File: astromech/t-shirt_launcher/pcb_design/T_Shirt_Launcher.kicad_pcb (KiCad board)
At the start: 2 copper layers, 15 parts, among them J1 Conn_01x02_Socket, J2 Conn_01x02_Socket, U1 ESP32-C6-DEVKITC-1-N8, U2 D36V50F5_Pololu, U3 ADA4510-2ARZ, U4 ADA4510-2ARZ, U5 MAX22203AUU+, U6 ADP3634ARDZ, U7 SN74LVC1G19DBVR, U8 SN74LVC1G19DBVR

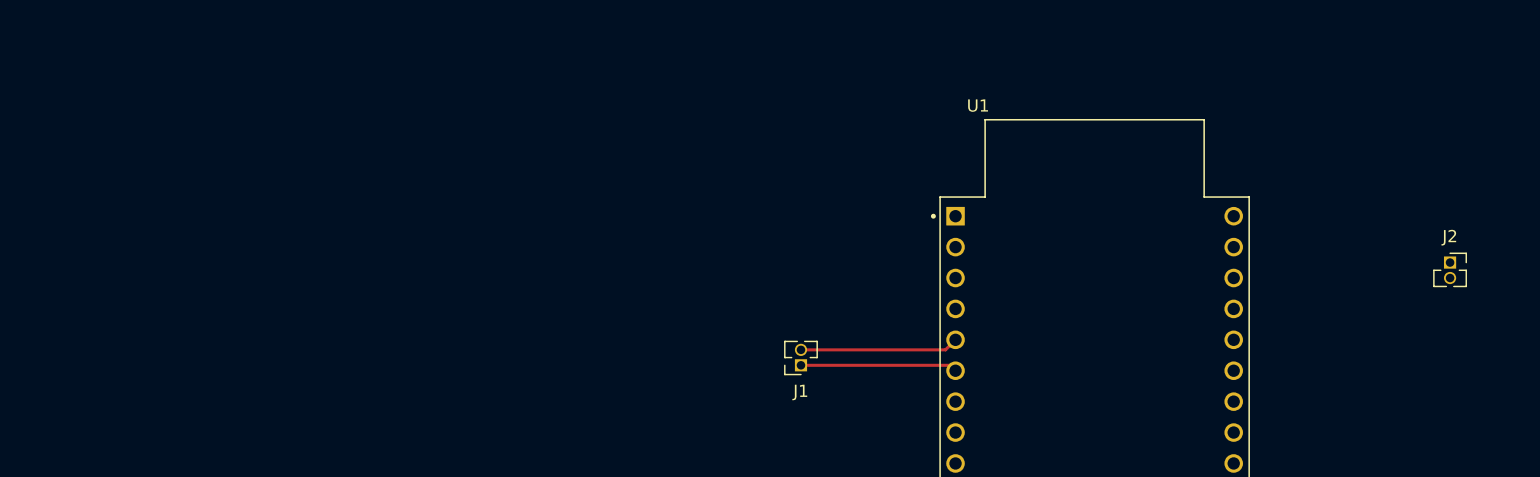
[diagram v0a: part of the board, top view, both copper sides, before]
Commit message: added some new parts and updated symbols to fit better on schematic
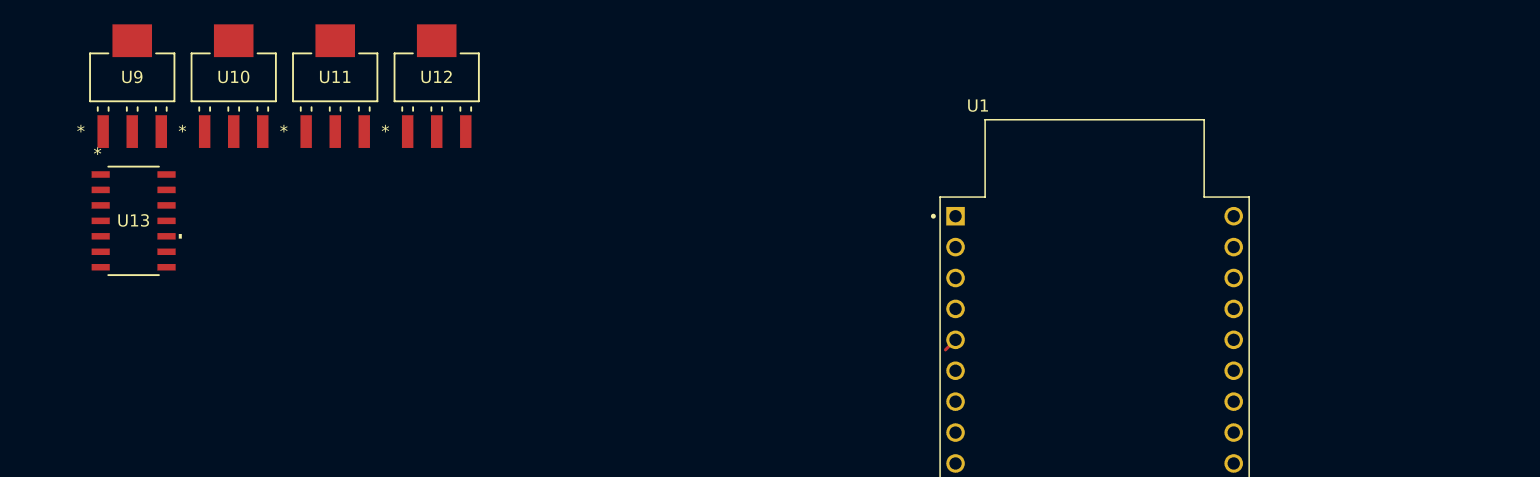
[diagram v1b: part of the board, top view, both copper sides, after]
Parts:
- removed J1, J2: Conn_01x02_Socket, Connector_PinSocket_1.27mm:PinSocket_1x02_P1.27mm_Vertical
- added U10: NTF3055L108T1G, NTF3055L108T1G:SOT-223_3P7X6P7_ONS, F.Cu at (98.2, 54.6)
- added U11: NTF3055L108T1G, NTF3055L108T1G:SOT-223_3P7X6P7_ONS, F.Cu at (106.5, 54.6)
- added U12: NTF3055L108T1G, NTF3055L108T1G:SOT-223_3P7X6P7_ONS, F.Cu at (114.8, 54.6)
- added U13: MC74HCU04ADG, MC74HCU04ADG:SOIC-14_NB_ONS, F.Cu at (89.9, 66.4)
- added U9: NTF3055L108T1G, NTF3055L108T1G:SOT-223_3P7X6P7_ONS, F.Cu at (89.8, 54.6)
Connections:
- U1 pad J1_1: unconnected-(U1-ESP_3V3-PadJ1_1) -> 3.3v
- U1 pad J1_5: sda -> unconnected-(U1-GPIO6-PadJ1_5)
- U1 pad J1_6: scl -> unconnected-(U1-GPIO7-PadJ1_6)
- U1 pad J3_2: txd -> unconnected-(U1-UART_TXD-PadJ3_2)
- U1 pad J3_3: rxd -> unconnected-(U1-UART_RXD-PadJ3_3)
- U1 pad J3_6: unconnected-(U1-GPIO22-PadJ3_6) -> Net-(J1-Pin_1)
- U1 pad J3_7: unconnected-(U1-GPIO21-PadJ3_7) -> Net-(J1-Pin_2)
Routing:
- net sda: track 13.0 -> 0.00 mm
- net scl: track 12.9 -> 0.00 mm
- net unconnected-(U1-GPIO6-PadJ1_5): track 0.00 -> 1.17 mm
- net unconnected-(U1-GPIO7-PadJ1_6): track 0.00 -> 0.63 mm
